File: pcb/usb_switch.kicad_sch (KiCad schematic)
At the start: 24 parts, among them J2 Conn_01x04_Socket, U1 FE1.1s, U14 USBLC6-2SC6, U2 24LC02, Y1 ABM8G-12.000MHZ-18

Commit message: More routing
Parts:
- D1, D2: value ~ -> (none)

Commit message: Add design review docs, expand README, sync PCB routing and production outputs
Routing progress on schematic/PCB, generated production outputs (gerbers,
BOM, PDFs), 3D model cache, and datasheet sync. Adds doc/ (design review
report + TODO) and README overview of architecture/status/repo layout.
Analysis tool output moved to .gitignore (regenerable, not source).
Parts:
- C2, C6: footprint Capacitor_SMD:C_0603_1608Metric_Pad1.08x0.95mm_HandSolder -> Capacitor_SMD:C_0603_1608Metric
- C3, C4, C5: footprint Capacitor_SMD:C_1206_3216Metric_Pad1.33x1.80mm_HandSolder -> Capacitor_SMD:C_1206_3216Metric
- D1, D2: footprint LED_SMD:LED_0603_1608Metric_Pad1.05x0.95mm_HandSolder -> LED_SMD:LED_0603_1608Metric
- R1, R10, R2, R3, R4, R5, R6, R7, R8, R9: footprint Resistor_SMD:R_0603_1608Metric_Pad0.98x0.95mm_HandSolder -> Resistor_SMD:R_0603_1608Metric
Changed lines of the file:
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@@
 	)
 	(junction
+		(at 71.12 44.45)
+		(diameter 0)
+		(color 0 0 0 0)
+	)
+	(junction
 		(at 189.23 81.28)
 		(diameter 0)
@@
 	)
 	(junction
-		(at 114.3 111.76)
-		(diameter 0)
-		(color 0 0 0 0)
-	)
-	(junction
 		(at 149.86 59.69)
 		(diameter 0)
@@
 	(wire
 		(pts
-			(xy 114.3 111.76) (xy 114.3 110.49)
-		)
-		(stroke
-			(width 0)
-			(type default)
-		)
-	)
-	(wire
-		(pts
 			(xy 52.07 77.47) (xy 45.72 77.47)
 		)
@@
 	(wire
 		(pts
-			(xy 114.3 100.33) (xy 114.3 99.06)
-		)
-		(stroke
-			(width 0)
-			(type default)
-		)
-	)
-	(wire
-		(pts
 			(xy 220.98 100.33) (xy 218.44 100.33)
 		)
@@
 	(wire
 		(pts
+			(xy 71.12 43.18) (xy 71.12 44.45)
+		)
+		(stroke
+			(width 0)
+			(type default)
+		)
+	)
+	(wire
+		(pts
 			(xy 52.07 80.01) (xy 52.07 77.47)
 		)
@@
 	(wire
 		(pts
-			(xy 119.38 99.06) (xy 119.38 111.76)
-		)
-		(stroke
-			(width 0)
-			(type default)
-		)
-	)
-	(wire
-		(pts
 			(xy 101.6 80.01) (xy 99.06 80.01)
 		)
@@
 	(wire
 		(pts
-			(xy 114.3 123.19) (xy 114.3 111.76)
+			(xy 114.3 110.49) (xy 114.3 123.19)
 		)
 		(stroke
@@
 	(wire
 		(pts
-			(xy 114.3 99.06) (xy 119.38 99.06)
-		)
-		(stroke
-			(width 0)
-			(type default)
-		)
-	)
-	(wire
-		(pts
 			(xy 160.02 100.33) (xy 179.07 100.33)
 		)
@@
 	(wire
 		(pts
-			(xy 119.38 111.76) (xy 114.3 111.76)
-		)
-		(stroke
-			(width 0)
-			(type default)
-		)
-	)
-	(wire
-		(pts
 			(xy 208.28 81.28) (xy 220.98 81.28)
 		)
@@
 			)
 		)
-		(property "Footprint" "Capacitor_SMD:C_1206_3216Metric_Pad1.33x1.80mm_HandSolder"
+		(property "Footprint" "Capacitor_SMD:C_1206_3216Metric"
 			(at 131.7752 53.34 0)
 			(hide yes)
@@
 			)
 		)
-		(property "Footprint" "Capacitor_SMD:C_0603_1608Metric_Pad1.08x0.95mm_HandSolder"
+		(property "Footprint" "Capacitor_SMD:C_0603_1608Metric"
 			(at 221.9452 90.17 0)
 			(hide yes)
@@
 			)
 		)
-		(property "Footprint" "LED_SMD:LED_0603_1608Metric_Pad1.05x0.95mm_HandSolder"
+		(property "Footprint" "LED_SMD:LED_0603_1608Metric"
 			(at 181.61 90.17 0)
 			(hide yes)
@@
 	)
 	(symbol
+		(lib_id "power:PWR_FLAG")
+		(at 71.12 43.18 0)
+		(unit 1)
+		(body_style 1)
+		(exclude_from_sim no)
+		(in_bom yes)
+		(on_board yes)
+		(in_pos_files yes)
+		(dnp no)
+		(property "Reference" "#FLG014"
+			(at 71.12 41.275 0)
+			(hide yes)
+			(show_name no)
+			(do_not_autoplace no)
+			(effects
+				(font
+					(size 1.27 1.27)
+				)
+			)
+		)
+		(property "Value" "PWR_FLAG"
+			(at 71.12 34.544 90)
+			(show_name no)
+			(do_not_autoplace no)
+			(effects
+				(font
+					(size 1.27 1.27)
+				)
+			)
+		)
+		(property "Footprint" ""
+			(at 71.12 43.18 0)
+			(hide yes)
+			(show_name no)
+			(do_not_autoplace no)
+			(effects
+				(font
+					(size 1.27 1.27)
+				)
+			)
+		)
+		(property "Datasheet" ""
+			(at 71.12 43.18 0)
+			(hide yes)
+			(show_name no)
+			(do_not_autoplace no)
+			(effects
+				(font
+					(size 1.27 1.27)
+				)
+			)
+		)
+		(property "Description" "Special symbol for telling ERC where power comes from"
+			(at 71.12 43.18 0)
+			(hide yes)
+			(show_name no)
+			(do_not_autoplace no)
+			(effects
+				(font
+					(size 1.27 1.27)
+				)
+			)
+		)
+		(pin "1"
+		)
+		(instances
+			(project "QCB_board"
+				(path "/3a9957e4-3d4a-4c65-a0c0-c287bc2a56fb/82a26402-3849-46fd-a3a1-52c735998b36"
+					(reference "#FLG014")
+					(unit 1)
+				)
+			)
+		)
+	)
+	(symbol
 		(lib_id "power:GND")
 		(at 85.09 80.01 0)
@@
 			)
 		)
-		(property "Footprint" "Capacitor_SMD:C_0603_1608Metric_Pad1.08x0.95mm_HandSolder"
+		(property "Footprint" "Capacitor_SMD:C_0603_1608Metric"
 			(at 120.3452 53.34 0)
 			(hide yes)
@@
 			)
 		)
-		(property "Footprint" "Resistor_SMD:R_0603_1608Metric_Pad0.98x0.95mm_HandSolder"
+		(property "Footprint" "Resistor_SMD:R_0603_1608Metric"
 			(at 187.452 90.17 90)
 			(hide yes)
@@
 			)
 		)
-		(property "Footprint" "Resistor_SMD:R_0603_1608Metric_Pad0.98x0.95mm_HandSolder"
+		(property "Footprint" "Resistor_SMD:R_0603_1608Metric"
 			(at 165.862 123.19 90)
 			(hide yes)
@@
 			)
 		)
-		(property "Footprint" "Resistor_SMD:R_0603_1608Metric_Pad0.98x0.95mm_HandSolder"
+		(property "Footprint" "Resistor_SMD:R_0603_1608Metric"
 			(at 193.548 90.17 90)
 			(hide yes)
@@
 			)
 		)
-		(property "Footprint" "Resistor_SMD:R_0603_1608Metric_Pad0.98x0.95mm_HandSolder"
+		(property "Footprint" "Resistor_SMD:R_0603_1608Metric"
 			(at 86.868 73.66 90)
 			(hide yes)
@@
 			)
 		)
-		(property "Footprint" "Resistor_SMD:R_0603_1608Metric_Pad0.98x0.95mm_HandSolder"
+		(property "Footprint" "Resistor_SMD:R_0603_1608Metric"
 			(at 176.022 81.28 90)
 			(hide yes)
@@
 			)
 		)
-		(property "Footprint" "Resistor_SMD:R_0603_1608Metric_Pad0.98x0.95mm_HandSolder"
+		(property "Footprint" "Resistor_SMD:R_0603_1608Metric"
 			(at 111.76 80.772 90)
 			(hide yes)
@@
 			)
 		)
-		(property "Footprint" "Resistor_SMD:R_0603_1608Metric_Pad0.98x0.95mm_HandSolder"
+		(property "Footprint" "Resistor_SMD:R_0603_1608Metric"
 			(at 183.388 81.28 90)
 			(hide yes)
@@
 			)
 		)
-		(property "Footprint" "Resistor_SMD:R_0603_1608Metric_Pad0.98x0.95mm_HandSolder"
+		(property "Footprint" "Resistor_SMD:R_0603_1608Metric"
 			(at 123.698 118.11 90)
 			(hide yes)
@@
 			)
 		)
-		(property "Footprint" "Resistor_SMD:R_0603_1608Metric_Pad0.98x0.95mm_HandSolder"
+		(property "Footprint" "Resistor_SMD:R_0603_1608Metric"
 			(at 105.41 78.232 90)
 			(hide yes)
@@
 			)
 		)
-		(property "Footprint" "Capacitor_SMD:C_1206_3216Metric_Pad1.33x1.80mm_HandSolder"
+		(property "Footprint" "Capacitor_SMD:C_1206_3216Metric"
 			(at 154.6352 53.34 0)
 			(hide yes)
@@
 			)
 		)
-		(property "Footprint" "LED_SMD:LED_0603_1608Metric_Pad1.05x0.95mm_HandSolder"
+		(property "Footprint" "LED_SMD:LED_0603_1608Metric"
 			(at 167.64 113.03 0)
 			(hide yes)
@@
 			)
 		)
-		(property "Footprint" "Resistor_SMD:R_0603_1608Metric_Pad0.98x0.95mm_HandSolder"
+		(property "Footprint" "Resistor_SMD:R_0603_1608Metric"
 			(at 76.2 68.072 90)
 			(hide yes)
@@
 			)
 		)
-		(property "Footprint" "Capacitor_SMD:C_1206_3216Metric_Pad1.33x1.80mm_HandSolder"
+		(property "Footprint" "Capacitor_SMD:C_1206_3216Metric"
 			(at 141.9352 53.34 0)
 			(hide yes)

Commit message: Unify passive values/footprints, add via-in-pad DRC rule, regen outputs
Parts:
- R1: value 0R/47k -> 0R
- R9: value 2k7 -> 2.7k
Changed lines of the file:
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@@
 			)
 		)
-		(property "Value" "2k7"
+		(property "Value" "2.7k"
 			(at 124.46 119.3799 0)
 			(show_name no)
@@
 			)
 		)
-		(property "Value" "0R/47k"
+		(property "Value" "0R"
 			(at 77.4699 67.31 0)
 			(show_name no)

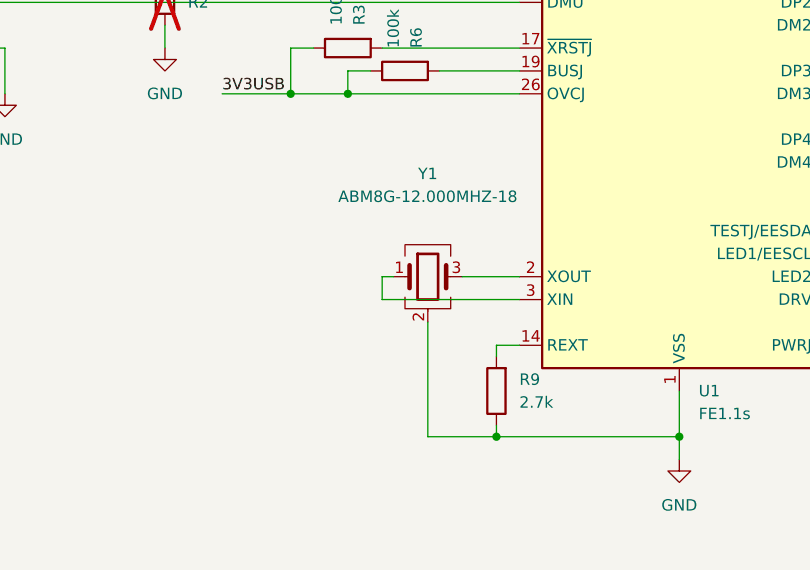
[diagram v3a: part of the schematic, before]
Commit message: Apply review checklist fixes, add fiducials, regenerate production outputs
- C41/C42 (Y2 load caps) now included in BOM
- Add USB hub crystal load caps C50/C51 (DNP), rework Y1 area placement
- 2 fiducials per side (hand assembly)
- Add IP175G, FE1.1s and UT8413A datasheets to doc/datasheet
- README: status updated (ready for prototype order), production links
- .gitignore: drop leftover SCA_board ibom.config.ini entry
- Regenerate BOM, PDFs, gerber zip, interactive BOM and 3D renders
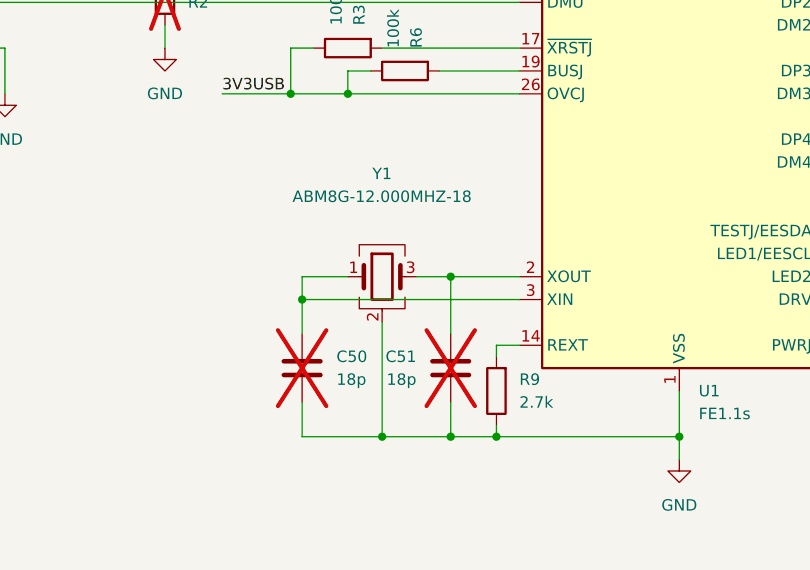
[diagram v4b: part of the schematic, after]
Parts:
- added C50, C51: 18p, Capacitor_SMD:C_0402_1005Metric, symbol Device:C
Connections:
- net GND: now also C50.2, C51.2
- net at U1.3 (XIN), Y1.1: now also C50.1
- net at U1.2 (XOUT), Y1.3: now also C51.1
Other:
- moved on the sheet: Y1
